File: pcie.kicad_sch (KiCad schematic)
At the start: 9 parts, among them U1 MPFS250T-FCVG484

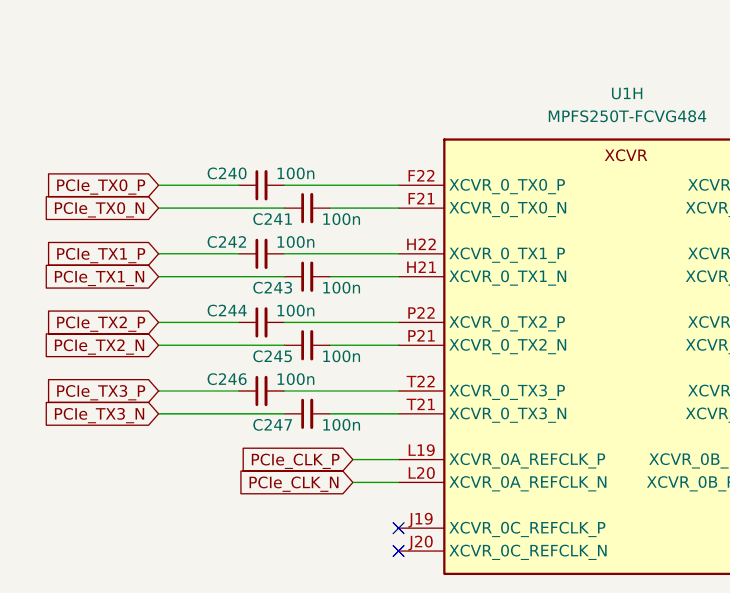
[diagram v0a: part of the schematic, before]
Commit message: [#55992] Replace 100n capacitors
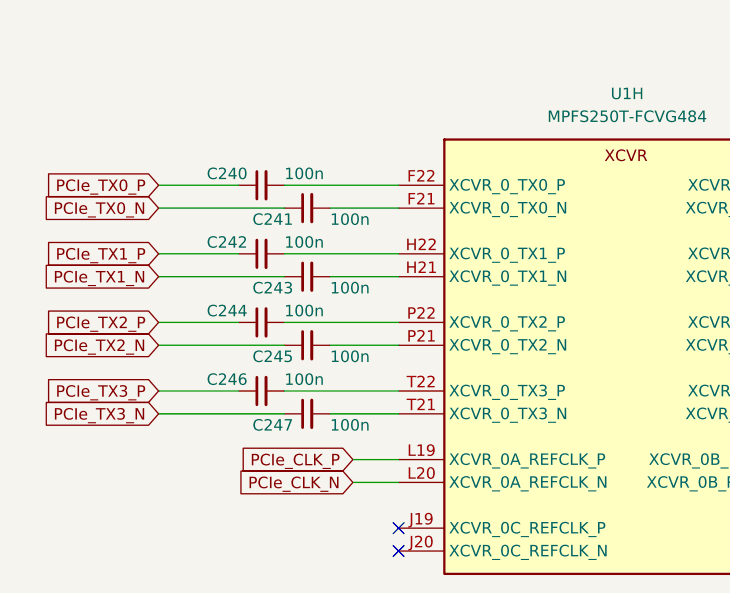
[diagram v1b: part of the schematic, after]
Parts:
- C240, C241, C242, C243, C244, C245, C246, C247: value C_100n_0201_25V -> C_100n_0402; footprint antmicro-footprints:C_0201 -> antmicro-footprints:C_0402_1005Metric; symbol antmicroCapacitorsmisc:C_100n_0201_25V -> antmicroCapacitors0402:C_100n_0402; Dielectric (none) -> X5R; MPN C0603X5R1E104K030BB -> GRM155R61H104KE14D; Manufacturer TDK -> Murata; Voltage 25V -> 50V

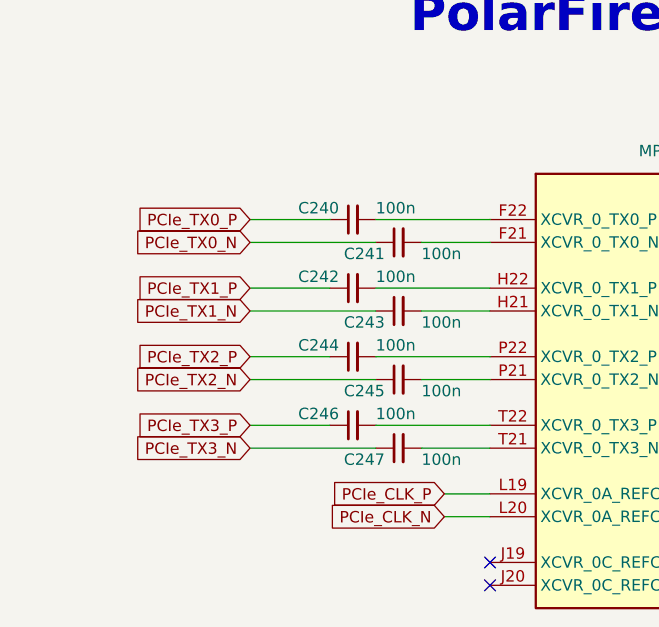
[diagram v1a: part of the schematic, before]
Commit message: [#56264] Add 4x100nF array and more GND via
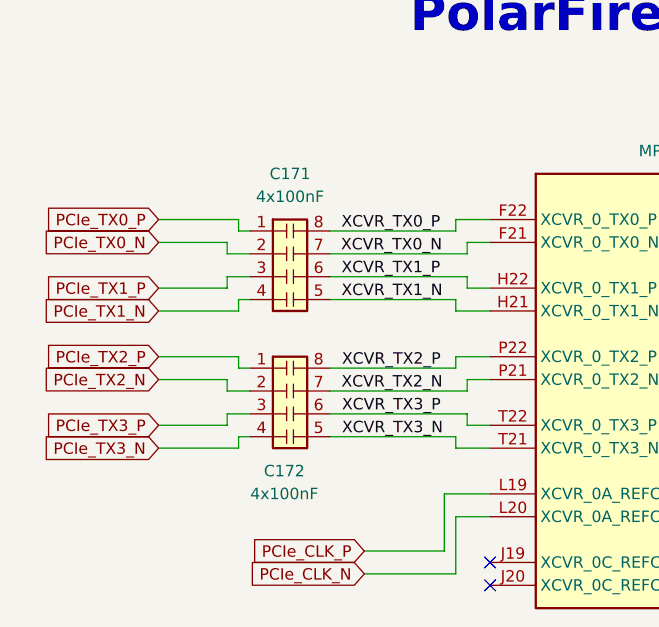
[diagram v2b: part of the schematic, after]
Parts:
- removed C240, C241, C242, C243, C244, C245, C246, C247: C_100n_0402, antmicro-footprints:C_0402_1005Metric, symbol antmicroCapacitors0402:C_100n_0402
- added C171, C172: C_4x100nF_0508_1220Metric_array, antmicro-footprints:C_Array_0508_1220Metric, symbol antmicroCapacitorsmisc:C_4x100nF_0508_1220Metric_array
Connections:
- net PCIe_TX0_N: now also C171.2 (R2.1)
- net PCIe_TX0_P: now also C171.1 (R1.1)
- net PCIe_TX1_N: now also C171.4 (R4.1)
- net PCIe_TX1_P: now also C171.3 (R3.1)
- net PCIe_TX2_N: now also C172.2 (R2.1)
- net PCIe_TX2_P: now also C172.1 (R1.1)
- net PCIe_TX3_N: now also C172.4 (R4.1)
- net PCIe_TX3_P: now also C172.3 (R3.1)
- net XCVR_TX3_N: now reaches U1.T21 (XCVR_0_TX3_N)
- net XCVR_TX3_N: now also C172.5 (R4.2)
- net XCVR_TX1_P: now reaches U1.H22 (XCVR_0_TX1_P)
- net XCVR_TX1_P: now also C171.6 (R3.2)
- net XCVR_TX2_N: now reaches U1.P21 (XCVR_0_TX2_N)
- net XCVR_TX2_N: now also C172.7 (R2.2)
- net XCVR_TX1_N: now reaches U1.H21 (XCVR_0_TX1_N)
- net XCVR_TX1_N: now also C171.5 (R4.2)
- net XCVR_TX0_P: now reaches U1.F22 (XCVR_0_TX0_P)
- net XCVR_TX0_P: now also C171.8 (R1.2)
- net XCVR_TX0_N: now reaches U1.F21 (XCVR_0_TX0_N)
- net XCVR_TX0_N: now also C171.7 (R2.2)
- net XCVR_TX3_P: now reaches U1.T22 (XCVR_0_TX3_P)
- net XCVR_TX3_P: now also C172.6 (R3.2)
- net XCVR_TX2_P: now reaches U1.P22 (XCVR_0_TX2_P)
- net XCVR_TX2_P: now also C172.8 (R1.2)

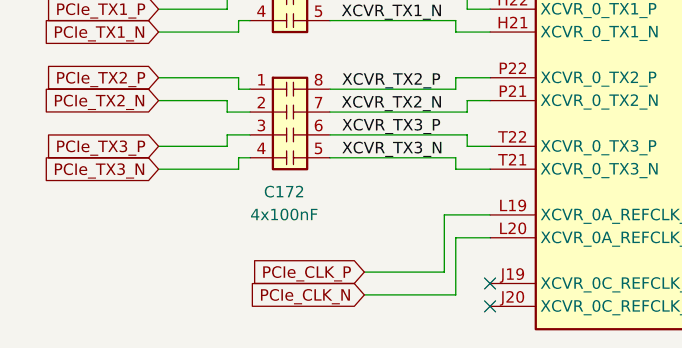
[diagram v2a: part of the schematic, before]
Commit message: [#57038] Add clock sources and logic shifters, change ETH PHY supply
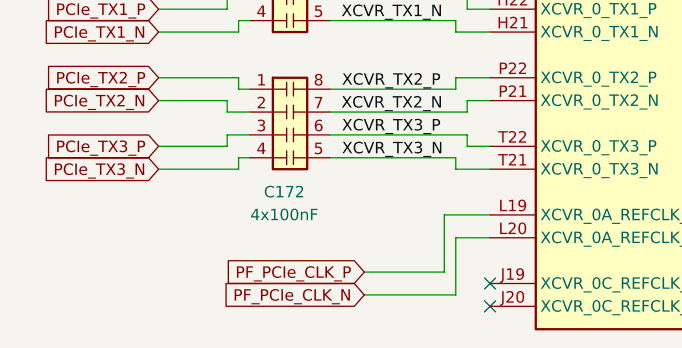
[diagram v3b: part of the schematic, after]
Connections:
- net PCIe_CLK_N renamed PF_PCIe_CLK_N
- net PCIe_CLK_P renamed PF_PCIe_CLK_P
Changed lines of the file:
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@@
     (effects (font (size 1.27 1.27)) (justify left bottom))
   )
-  (global_label "PCIe_CLK_N" (shape input) (at 163.83 157.48 180) (fields_autoplaced)
+  (global_label "PF_PCIe_CLK_N" (shape input) (at 163.83 157.48 180) (fields_autoplaced)
     (effects (font (size 1.27 1.27)) (justify right))
-    (property "Intersheetrefs" "${INTERSHEET_REFS}" (at 150.3498 157.4006 0)
+    (property "Intersheetrefs" "${INTERSHEET_REFS}" (at 146.4514 157.48 0)
       (effects (font (size 1.27 1.27)) (justify right) hide)
     )
@@
     )
   )
+  (global_label "PF_PCIe_CLK_P" (shape input) (at 163.83 154.94 180) (fields_autoplaced)
+    (effects (font (size 1.27 1.27)) (justify right))
+    (property "Intersheetrefs" "${INTERSHEET_REFS}" (at 146.5119 154.94 0)
+      (effects (font (size 1.27 1.27)) (justify right) hide)
+    )
+  )
   (global_label "PCIe_RX2_N" (shape input) (at 233.68 135.89 0) (fields_autoplaced)
     (effects (font (size 1.27 1.27)) (justify left))
@@
       (effects (font (size 1.27 1.27)) (justify right) hide)
     )
-  )
-  (global_label "PCIe_CLK_P" (shape input) (at 163.83 154.94 180) (fields_autoplaced)
-    (effects (font (size 1.27 1.27)) (justify right))
-    (property "Intersheetrefs" "${INTERSHEET_REFS}" (at 150.4102 154.8606 0)
-      (effects (font (size 1.27 1.27)) (justify right) hide)
-    )

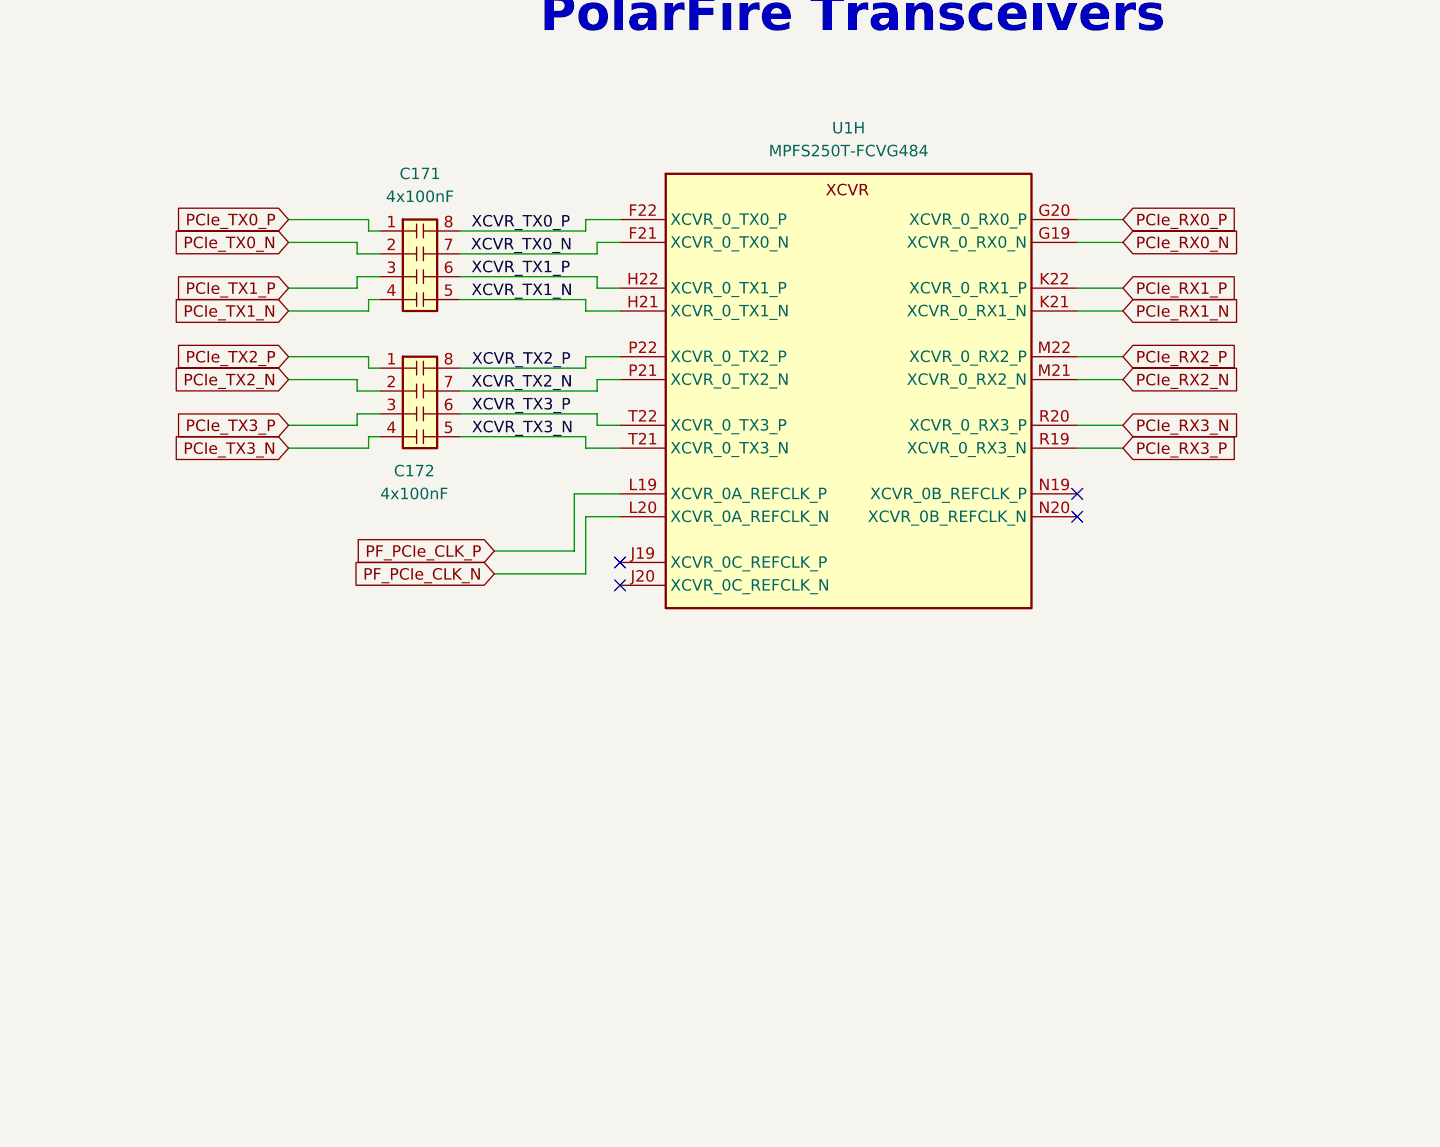
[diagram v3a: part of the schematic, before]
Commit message: [#57505] Start reworking schematic to hierarchical structure
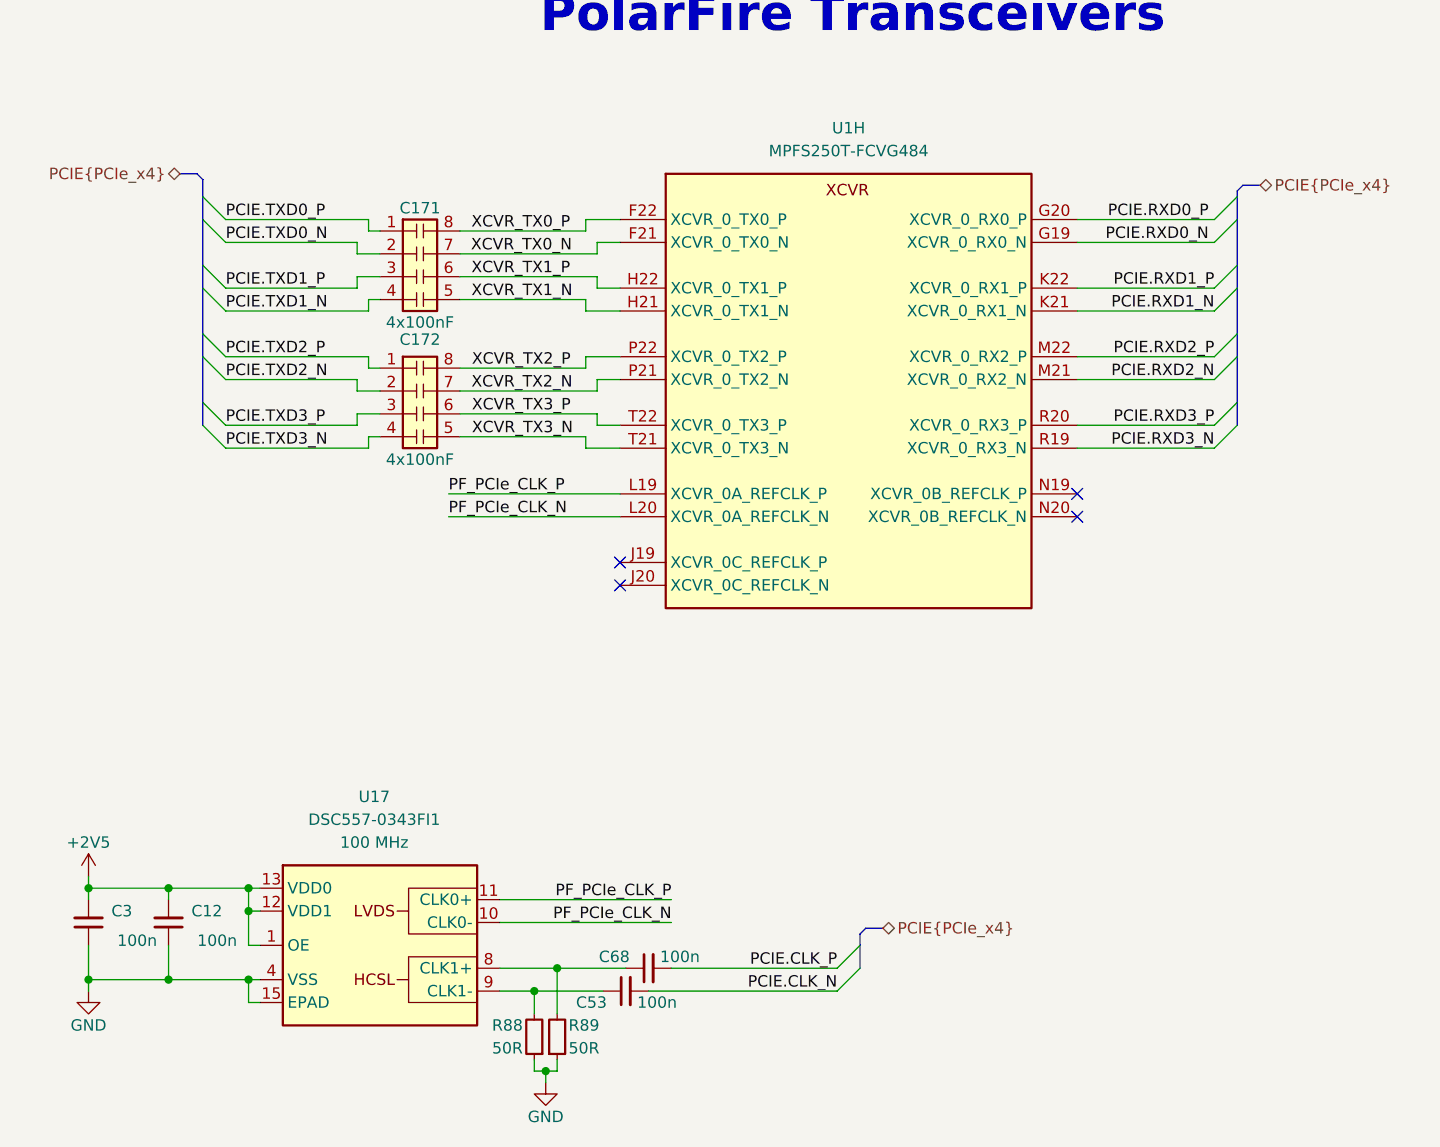
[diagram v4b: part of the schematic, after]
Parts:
- added C12, C3, C53, C68: C_100n_0402, antmicro-footprints:C_0402_1005Metric, symbol antmicroCapacitors0402:C_100n_0402
- added R88, R89: R_50R_0402, antmicro-footprints:R_0402_1005Metric, symbol antmicroResistors0402:R_50R_0402
- added U17: DSC557-0343FI1, antmicro-footprints:VQFN-14-1EP_3.2x2.5mm_P0.5mm_Layout4x3, symbol antmicroClockTimingRealTimeClocks:DSC557-0343FI1
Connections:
- net PF_PCIe_CLK_N: now also U17.10 (CLK0-)
- net PF_PCIe_CLK_P: now also U17.11 (CLK0+)
- net PCIe_RX0_N renamed PCIE.RXD0_N
- net PCIe_RX0_P renamed PCIE.RXD0_P
- net PCIe_RX1_N renamed PCIE.RXD1_N
- net PCIe_RX1_P renamed PCIE.RXD1_P
- net PCIe_RX2_N renamed PCIE.RXD2_N
- net PCIe_RX2_P renamed PCIE.RXD2_P
- net PCIe_RX3_N renamed PCIE.RXD3_P
- net PCIe_RX3_P renamed PCIE.RXD3_N
- net PCIe_TX0_N renamed PCIE.TXD0_N
- net PCIe_TX0_P renamed PCIE.TXD0_P
- net PCIe_TX1_N renamed PCIE.TXD1_N
- net PCIe_TX1_P renamed PCIE.TXD1_P
- net PCIe_TX2_N renamed PCIE.TXD2_N
- net PCIe_TX2_P renamed PCIE.TXD2_P
- net PCIe_TX3_N renamed PCIE.TXD3_N
- net PCIe_TX3_P renamed PCIE.TXD3_P
- new net: C53.1, R88.2, U17.9 (CLK1-)
- new net: C68.1, R89.2, U17.8 (CLK1+)
- new net: U17.14 (NC), U17.2 (NC), U17.3 (NC), U17.5 (NC), U17.6 (NC), U17.7 (NC)
- new net +2V5: C12.2, C3.2, U17.1 (OE), U17.12 (VDD1), U17.13 (VDD0)
- new net GND: C12.1, C3.1, R88.1, R89.1, U17.15 (EPAD), U17.4 (VSS)
- new net PCIE.CLK_N: C53.2
- new net PCIE.CLK_P: C68.2

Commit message: [#57422] Finishing touches
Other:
- note added: "PolarFire XCVR"
- note removed: "PolarFire Transceivers"
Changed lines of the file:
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@@
   (title_block
     (title "PolarFire SoM")
-    (date "2024-04-03")
+    (date "2024-04-08")
     (rev "1.0.0")
     (company "Antmicro Ltd")
@@
     )
   )
-  (text "PolarFire Transceivers" (at 168.91 97.79 0)
+  (text "PolarFire XCVR" (at 15.24 21.59 0)
     (effects (font (size 4 4) (thickness 0.8) bold) (justify left bottom))
   )
